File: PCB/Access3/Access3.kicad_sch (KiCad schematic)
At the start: 71 parts, among them J1 USB-C, J2 RFID, J3 INPUTS, J4 Shelly, J5 POWER, J6 DOOR, Q1 NX7002AK, Q2 PMF250XNEX, SW1 ESE13V01D, U1 ESP32-PICO-MINI-02, U2 FT231XQ, U3 G3VM-41GR8, U4 LMR16006XDDCR, U5 LMR16006XDDCR, U6 AA, U7 QR

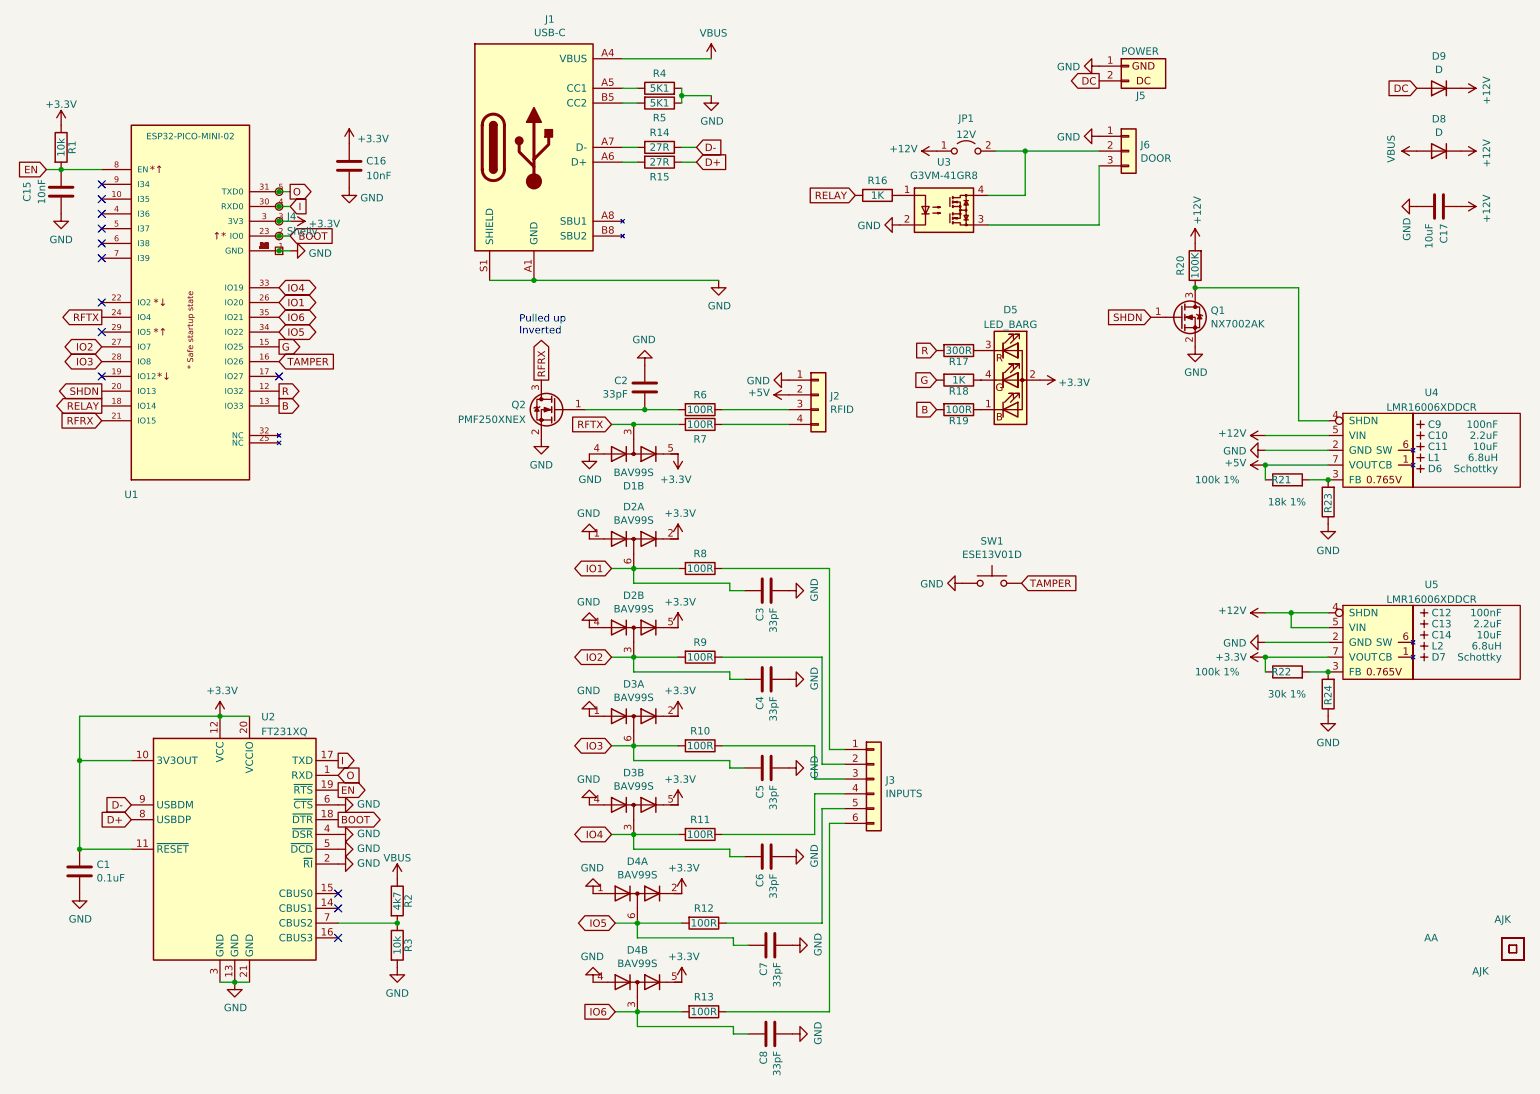
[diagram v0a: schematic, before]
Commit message: Started new board with two relay outputs
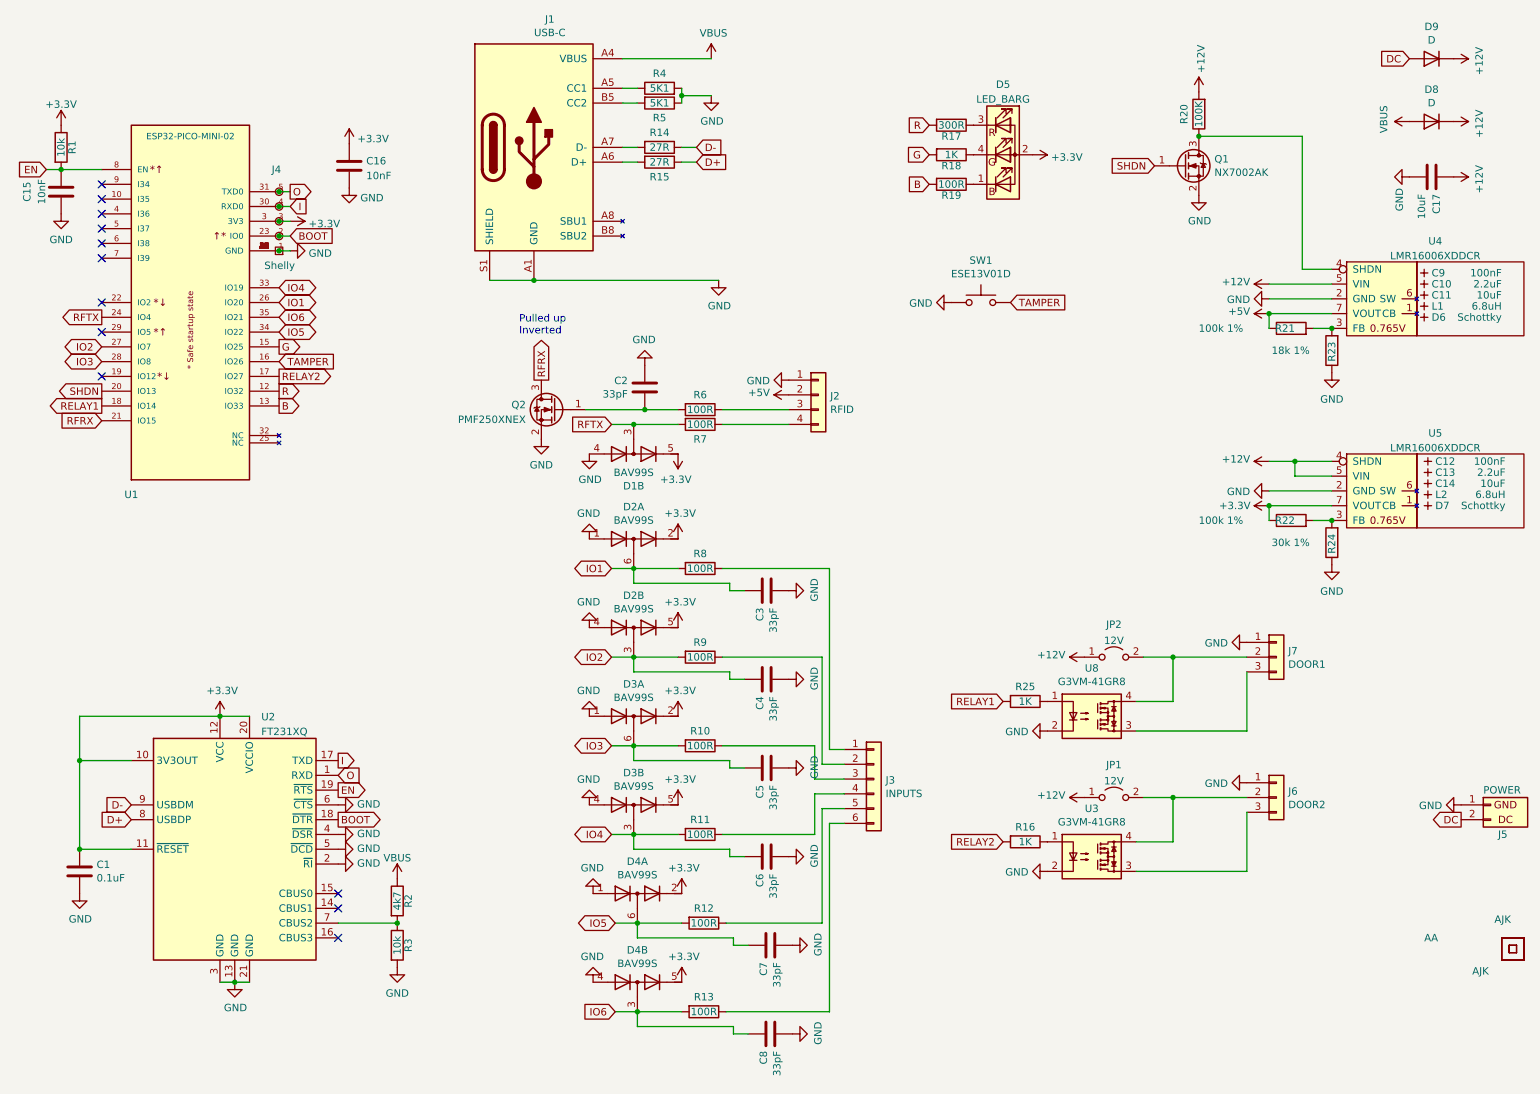
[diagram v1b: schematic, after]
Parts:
- added J7: DOOR1, RevK:Molex_MiniSPOX_H3RA, symbol Connector_Generic:Conn_01x03
- added JP2: 12V, Jumper:SolderJumper-2_P1.3mm_Open_RoundedPad1.0x1.5mm, symbol Jumper:Jumper_2_Open
- added R25: 1K, RevK:R_0603, symbol Device:R
- added U8: G3VM-41GR8, RevK:Special-SOP-4-3.7x4.55, symbol RevK:G3VM-41GR8
- J6: value DOOR -> DOOR2
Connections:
- net +12V: now also JP2.1 (A)
- net GND: now also J7.1 (Pin_1), U8.2
- net RELAY2: now reaches U1.17 (IO27)
- net RELAY2: now also R16.2
- net RELAY renamed RELAY1
- net RELAY1: now also R25.2; no longer R16.2
- new net: J7.2 (Pin_2), JP2.2 (B), U8.4
- new net: R25.1, U8.1
- new net: J7.3 (Pin_3), U8.3
- no-connect marks 13 -> 12
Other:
- moved on the sheet: C10, C11, C12, C13, C14, C17, C9, D5, D6, D7, D8, D9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

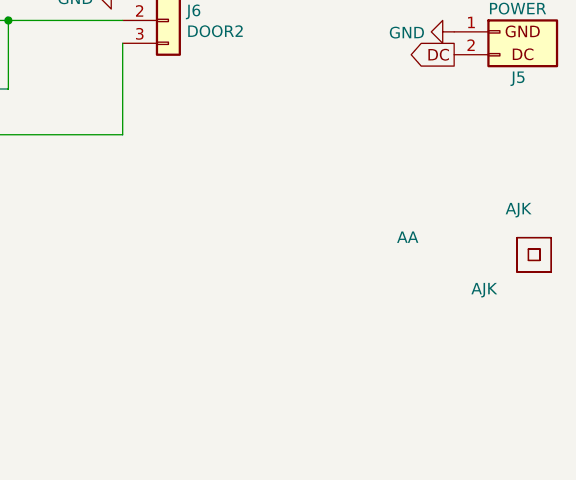
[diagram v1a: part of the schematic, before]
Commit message: New dual output board
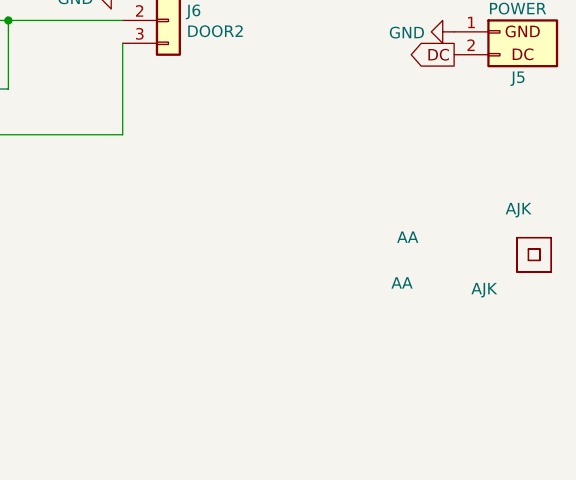
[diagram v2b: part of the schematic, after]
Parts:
- added U9: AA, RevK:AA, symbol RevK:AA
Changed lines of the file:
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@@
     (pin "1")
+  )
+  (symbol (lib_id "RevK:AA") (at 257.81 177.8 0) (unit 1)
+    (in_bom no) (on_board yes)
+    (property "Reference" "U9" (id 0) (at 259.08 176.53 0)
+      (effects (font (size 1.27 1.27)) hide)
+    )
+    (property "Value" "AA" (id 1) (at 257.175 177.8 0)
+      (effects (font (size 1.27 1.27)) (justify left))
+    )
+    (property "Footprint" "RevK:AA" (id 2) (at 257.81 177.8 0)
+      (effects (font (size 1.27 1.27)) hide)
+    )
+    (property "Datasheet" "" (id 3) (at 257.81 177.8 0)
+      (effects (font (size 1.27 1.27)) hide)
+    )
+    (property "Note" "Non part, PCB printed" (id 4) (at 257.81 177.8 0)
+      (effects (font (size 1.27 1.27)) hide)
+    )
   )
   (symbol (lib_id "RevK:Shelly") (at 60.96 49.53 0) (unit 1)
@@
       (reference "U8") (unit 1) (value "G3VM-41GR8") (footprint "RevK:Special-SOP-4-3.7x4.55")
     )
-  )
+    (path "/0479bcb3-8699-4b8f-bf33-b1f3d7685380"
+      (reference "U9") (unit 1) (value "AA") (footprint "RevK:AA")
+    )
+  )

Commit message: New cases
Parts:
- D6, D7, Q2: JLCPCB Rotation Offset 180 -> 0
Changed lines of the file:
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@@
       (effects (font (size 1.27 1.27)) hide)
     )
-    (property "JLCPCB Rotation Offset" "180" (id 7) (at 258.445 98.425 0)
+    (property "JLCPCB Rotation Offset" "0" (id 7) (at 258.445 98.425 0)
       (effects (font (size 1.27 1.27)) hide)
     )
@@
       (effects (font (size 1.27 1.27)) hide)
     )
-    (property "JLCPCB Rotation Offset" "180" (id 6) (at 108.585 81.915 0)
+    (property "JLCPCB Rotation Offset" "0" (id 6) (at 108.585 81.915 0)
       (effects (font (size 1.27 1.27)) hide)
     )
@@
       (effects (font (size 1.27 1.27)) hide)
     )
-    (property "JLCPCB Rotation Offset" "180" (id 7) (at 257.81 66.04 0)
-      (effects (font (size 1.27 1.27)) hide)
-    )
+    (property "JLCPCB Rotation Offset" "0" (id 7) (at 257.81 66.04 0)
+      (effects (font (size 1.27 1.27)) hide)
+    )

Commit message: PSTM connectors
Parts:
- J2: footprint RevK:Molex_MiniSPOX_H4RA -> RevK:PTSM-HH-4-RA
- J3: footprint RevK:Molex_MiniSPOX_H6RA -> RevK:PTSM-HH-6-RA
- J5: footprint RevK:Molex_MiniSPOX_H2RA -> RevK:PTSM-HH-2-RA
- J6, J7: footprint RevK:Molex_MiniSPOX_H3RA -> RevK:PTSM-HH-3-RA
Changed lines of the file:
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@@
       (effects (font (size 1.27 1.27)) (justify left))
     )
-    (property "Footprint" "RevK:Molex_MiniSPOX_H4RA" (id 2) (at 153.67 79.375 0)
+    (property "Footprint" "RevK:PTSM-HH-4-RA" (id 2) (at 153.67 79.375 0)
       (effects (font (size 1.27 1.27)) hide)
     )
@@
       (effects (font (size 1.27 1.27)) (justify left))
     )
-    (property "Footprint" "RevK:Molex_MiniSPOX_H2RA" (id 2) (at 269.24 149.86 0)
+    (property "Footprint" "RevK:PTSM-HH-2-RA" (id 2) (at 269.24 149.86 0)
       (effects (font (size 1.27 1.27)) hide)
     )
@@
       (effects (font (size 1.27 1.27)) (justify left))
     )
-    (property "Footprint" "RevK:Molex_MiniSPOX_H3RA" (id 2) (at 232.41 148.59 0)
+    (property "Footprint" "RevK:PTSM-HH-3-RA" (id 2) (at 232.41 148.59 0)
       (effects (font (size 1.27 1.27)) hide)
     )
@@
       (effects (font (size 1.27 1.27)) (justify left))
     )
-    (property "Footprint" "RevK:Molex_MiniSPOX_H6RA" (id 2) (at 163.195 145.415 0)
+    (property "Footprint" "RevK:PTSM-HH-6-RA" (id 2) (at 163.195 145.415 0)
       (effects (font (size 1.27 1.27)) hide)
     )
@@
       (effects (font (size 1.27 1.27)) (justify left))
     )
-    (property "Footprint" "RevK:Molex_MiniSPOX_H3RA" (id 2) (at 232.41 124.46 0)
+    (property "Footprint" "RevK:PTSM-HH-3-RA" (id 2) (at 232.41 124.46 0)
       (effects (font (size 1.27 1.27)) hide)
     )
@@
     )
     (path "/00000000-0000-0000-0000-000060739fa0"
-      (reference "J2") (unit 1) (value "RFID") (footprint "RevK:Molex_MiniSPOX_H4RA")
+      (reference "J2") (unit 1) (value "RFID") (footprint "RevK:PTSM-HH-4-RA")
     )
     (path "/00000000-0000-0000-0000-0000608cf414"
-      (reference "J3") (unit 1) (value "INPUTS") (footprint "RevK:Molex_MiniSPOX_H6RA")
+      (reference "J3") (unit 1) (value "INPUTS") (footprint "RevK:PTSM-HH-6-RA")
     )
     (path "/054d3fd2-4931-4b9d-baac-1a45d3fc9bae"
@@
     )
     (path "/00000000-0000-0000-0000-00006074263f"
-      (reference "J5") (unit 1) (value "POWER") (footprint "RevK:Molex_MiniSPOX_H2RA")
+      (reference "J5") (unit 1) (value "POWER") (footprint "RevK:PTSM-HH-2-RA")
     )
     (path "/00000000-0000-0000-0000-0000608cb396"
-      (reference "J6") (unit 1) (value "DOOR2") (footprint "RevK:Molex_MiniSPOX_H3RA")
+      (reference "J6") (unit 1) (value "DOOR2") (footprint "RevK:PTSM-HH-3-RA")
     )
     (path "/b0813172-89be-4441-9329-0960f03d38d2"
-      (reference "J7") (unit 1) (value "DOOR1") (footprint "RevK:Molex_MiniSPOX_H3RA")
+      (reference "J7") (unit 1) (value "DOOR1") (footprint "RevK:PTSM-HH-3-RA")
     )
     (path "/b9e3b3a7-ba8d-4414-9892-926f9909a922"

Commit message: White socket
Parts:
- J6: footprint RevK:PTSM-HH-3-RA -> RevK:PTSM-HH-3-RA-W
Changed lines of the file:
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@@
       (effects (font (size 1.27 1.27)) (justify left))
     )
-    (property "Footprint" "RevK:PTSM-HH-3-RA" (id 2) (at 232.41 148.59 0)
+    (property "Footprint" "RevK:PTSM-HH-3-RA-W" (id 2) (at 232.41 148.59 0)
       (effects (font (size 1.27 1.27)) hide)
     )
@@
     )
     (path "/00000000-0000-0000-0000-0000608cb396"
-      (reference "J6") (unit 1) (value "DOOR2") (footprint "RevK:PTSM-HH-3-RA")
+      (reference "J6") (unit 1) (value "DOOR2") (footprint "RevK:PTSM-HH-3-RA-W")
     )
     (path "/b0813172-89be-4441-9329-0960f03d38d2"

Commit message: Updated for locking smaller sockets
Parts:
- J5: footprint RevK:PTSM-HH-2-RA -> RevK:PTSM-HH1-2-RA
- J6: footprint RevK:PTSM-HH-3-RA-W -> RevK:PTSM-HH1-3-RA-W
- J7: footprint RevK:PTSM-HH-3-RA -> RevK:PTSM-HH1-3-RA
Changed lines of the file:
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@@
       (effects (font (size 1.27 1.27)) (justify left))
     )
-    (property "Footprint" "RevK:PTSM-HH-2-RA" (id 2) (at 269.24 149.86 0)
+    (property "Footprint" "RevK:PTSM-HH1-2-RA" (id 2) (at 269.24 149.86 0)
       (effects (font (size 1.27 1.27)) hide)
     )
@@
       (effects (font (size 1.27 1.27)) (justify left))
     )
-    (property "Footprint" "RevK:PTSM-HH-3-RA-W" (id 2) (at 232.41 148.59 0)
+    (property "Footprint" "RevK:PTSM-HH1-3-RA-W" (id 2) (at 232.41 148.59 0)
       (effects (font (size 1.27 1.27)) hide)
     )
@@
       (effects (font (size 1.27 1.27)) (justify left))
     )
-    (property "Footprint" "RevK:PTSM-HH-3-RA" (id 2) (at 232.41 124.46 0)
+    (property "Footprint" "RevK:PTSM-HH1-3-RA" (id 2) (at 232.41 124.46 0)
       (effects (font (size 1.27 1.27)) hide)
     )
@@
     )
     (path "/00000000-0000-0000-0000-00006074263f"
-      (reference "J5") (unit 1) (value "POWER") (footprint "RevK:PTSM-HH-2-RA")
+      (reference "J5") (unit 1) (value "POWER") (footprint "RevK:PTSM-HH1-2-RA")
     )
     (path "/00000000-0000-0000-0000-0000608cb396"
-      (reference "J6") (unit 1) (value "DOOR2") (footprint "RevK:PTSM-HH-3-RA-W")
+      (reference "J6") (unit 1) (value "DOOR2") (footprint "RevK:PTSM-HH1-3-RA-W")
     )
     (path "/b0813172-89be-4441-9329-0960f03d38d2"
-      (reference "J7") (unit 1) (value "DOOR1") (footprint "RevK:PTSM-HH-3-RA")
+      (reference "J7") (unit 1) (value "DOOR1") (footprint "RevK:PTSM-HH1-3-RA")
     )
     (path "/b9e3b3a7-ba8d-4414-9892-926f9909a922"

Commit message: Tidy
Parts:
- C15: value 10nF -> 1uF
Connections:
- no-connect marks 12 -> 13
